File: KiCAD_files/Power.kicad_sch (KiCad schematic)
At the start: 44 parts, among them J101 Wago 6 contacts, P101 Power2, U101 AMC1311, U102 MCP6486UT-E/LT, U103 MCP6486UT-E/LT, U104 ACS723LLCTR-20AB

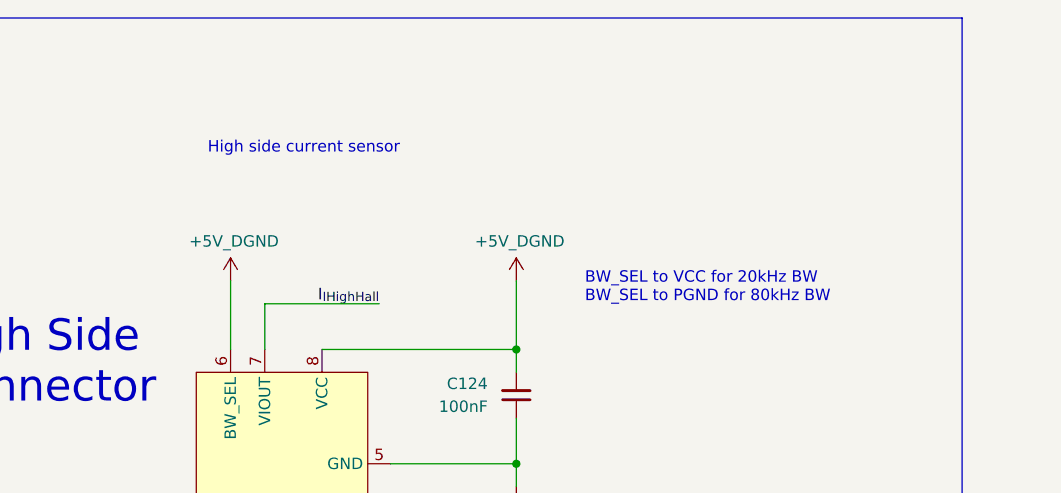
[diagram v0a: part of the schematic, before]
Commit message: better comments for ACS723 high side current sensor
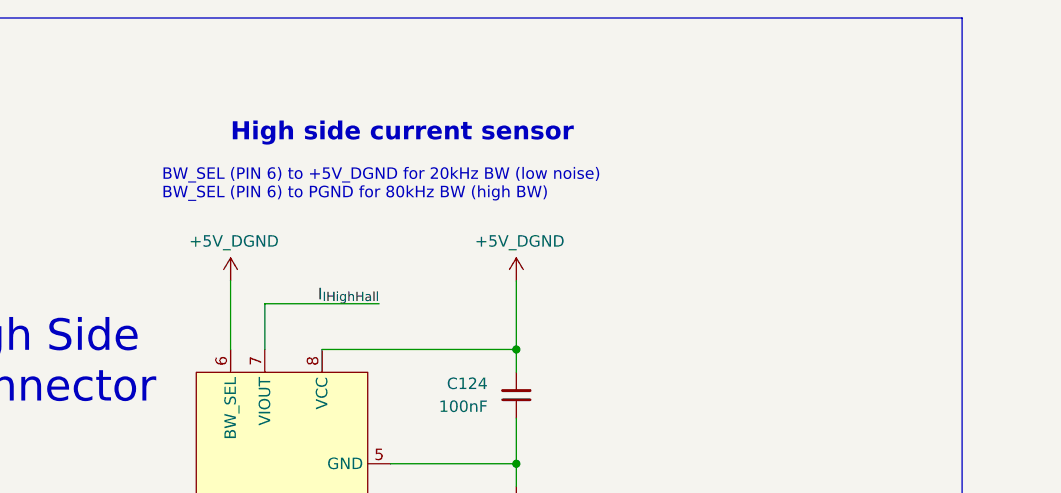
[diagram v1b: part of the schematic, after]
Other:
- note added: "BW_SEL (PIN 6) to +5V_DGND for 20kHz BW (low noise) BW_SEL (PIN 6) to PGND for 80kHz BW (high BW)"
- note removed: "BW_SEL to VCC for 20kHz BW BW_SEL to PGND for 80kHz BW"
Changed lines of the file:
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@@
     (effects (font (size 1.27 1.27)) (justify left bottom))
   )
-  (text "High side current sensor" (at 207.01 29.21 0)
-    (effects (font (size 1.27 1.27)) (justify left bottom))
+  (text "High side current sensor" (at 209.55 27.94 0)
+    (effects (font (size 2 2) (thickness 0.4) bold) (justify left bottom))
   )
   (text "V_High has no offset \nas V_High is solely positive\n"
@@
     (effects (font (size 1.27 1.27)) (justify left bottom))
   )
-  (text "BW_SEL to VCC for 20kHz BW\nBW_SEL to PGND for 80kHz BW"
-    (at 248.92 45.72 0)
+  (text "BW_SEL (PIN 6) to +5V_DGND for 20kHz BW (low noise)\nBW_SEL (PIN 6) to PGND for 80kHz BW (high BW)"
+    (at 201.93 34.29 0)
     (effects (font (size 1.27 1.27)) (justify left bottom))
   )

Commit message: wip SHEMATIC
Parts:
- removed C101, C102, C124: 100nF, Capacitor_SMD:C_1206_3216Metric, symbol Device:C_Small
- removed C103, C117, C123: 100nF, Footprints:C_0805_2012Metric, symbol Device:C_Small
- removed C106, C119: 20pF, Footprints:C_0805_2012Metric, symbol Device:C_Small
- removed R103, R104, R105, R107: 27k, Footprints:R_0805_2012Metric, symbol Device:R_Small
- removed R110, R116: 5.9k, Footprints:R_0805_2012Metric, symbol Device:R_Small
- removed R111, R115: 20k, Footprints:R_0805_2012Metric, symbol Device:R_Small
- removed R117: 330k, Footprints:R_0805_2012Metric, symbol Device:R_Small
- removed R118: 5.6k, Footprints:R_0805_2012Metric, symbol Device:R_Small
- removed TP101, TP102, TP103, TP104, TP105, TP106, TP107: TestPoint, Footprints:TestPoint_THTPad_D1.5mm_Drill0.7mm, symbol Connector:TestPoint
- removed U101: AMC1311, Footprints:SOIC-8_7.5x5.85mm_P1.27mm, symbol Symbols:AMC1311
- removed U102, U103: MCP6486UT-E/LT, Package_TO_SOT_SMD:SOT-353_SC-70-5_Handsoldering, symbol Amplifier_Operational:TLV6001DCK
- removed U104: ACS723LLCTR-20AB, Package_SO:SOIC-8_3.9x4.9mm_P1.27mm, symbol Symbols:ACS723
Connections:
- net NGND is gone; now on net PGND: J101.14 (Pin_4), J101.6 (Pin_1), J101.7 (Pin_2), J101.8 (Pin_3)
- net High_side/V_{IHighOutFused_PGND}: now reaches F103.2, J101.1 (Pin_1)
- net V1_Low renamed V1_Low_PGND
- net V2_Low renamed V2_Low_PGND
- net V_{IHighOut} renamed V_{IHighOut_PGND}
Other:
- sheet Digital renamed MCU
- added sheet High_side (High_side.kicad_sch)
- sheet Feeder ports: added VIN_PGND, Vref_DGND; removed +5V_NEUTRAL, VIN, VRef
- sheet MCU ports: added +3.3V_DGND, HRTIM_CHA1_DGND, HRTIM_CHA2_DGND, HRTIM_CHC1_DGND, HRTIM_CHC2_DGND, I_{I1Low_DGND}, I_{I2Low_DGND}, I_{IHigh_sense_DGND}, V_{I1Low_DGND}, V_{I2Low_DGND}, V_{IHigh_sense_DGND}, ~{STBY1}_DGND, ~{STBY2}_DGND; removed HRTIM_CHA1, HRTIM_CHA2, HRTIM_CHC1, HRTIM_CHC2, I_{I1Low}, I_{I2Low}, I_{IHigh}, N_{PGND}, VREF, V_{I1Low}, V_{I2Low}, V_{IHighfeeder}, V_{IHigh}, ~{STBY1}, ~{STBY2}
- sheet Power Leg 1 ports: added HRTIM_HIGH_DGND, HRTIM_LOW_DGND, I_{ILow_DGND}, V_High_PGND, V_Low_PGND, V_{ILow_DGND}, ~{STBY}_DGND; removed HRTIM1_CH1, HRTIM1_CH2, I_{ILow}, N_{PGND}, VRef, V_High, V_Low, V_{ILow}, ~{STBY}
- sheet Power Leg 2 ports: added HRTIM_HIGH_DGND, HRTIM_LOW_DGND, I_{ILow_DGND}, V_High_PGND, V_Low_PGND, V_{ILow_DGND}, ~{STBY}_DGND; removed HRTIM1_CH1, HRTIM1_CH2, I_{ILow}, N_{PGND}, VRef, V_High, V_Low, V_{ILow}, ~{STBY}
- note added: "All resistor are thick film 1/8Watt unless specified"
- note added: "High Side"
- note added: "designator base 200"
- note added: "designator base 300"
- note added: "designator base 400"
- note added: "designator base 500"
- note added: "designator base 600"
- note removed: "All resistor to are thick film 1/8Watt unless specified"
- note removed: "BW_SEL (PIN 6) to +5V_DGND for 20kHz BW (low noise) BW_SEL (PIN 6) to PGND for 80kHz BW (high BW)"
- note removed: "Circuit can be seen as non inverting opamp with gain : G = 1+(RC/RD) and a potential on non-inverting input equal to V+=(VOUTP-VOUTN) multiplied by the ratio of voltage divider equal to : r = RB/(RA+RB)"
- note removed: "Current measurements 5V to 2.048"
- note removed: "Gain : 1"
- note removed: "High Side Current Measure"
- note removed: "High Side Voltage Measure"
- note removed: "High Side voltage measurement"
- note removed: "High side current sensor"
- note removed: "NEUTRAL AREA"
- note removed: "RA"
- note removed: "RB"
- note removed: "RC"
- note removed: "RD"
- note removed: "RE"
- note removed: "RF"
- note removed: "RG"
- note removed: "RH"
- note removed: "Simulation available https://tinyurl.com/2k73em8x"
- note removed: "VI_High_op has a 2,048V amplitude without offset"
- note removed: "V_High has no offset as V_High is solely positive"
- note removed: "V_{SHIFTED} = ((RE + RF)*RH / (RH + RG)*RF) * I_{IHigh} - (RE/RF)* 5V_{Digital} V_{SHIFTED} = ((5.9k + 20k)*20k / (20k + 5.9k)*20k) * I_{IHigh} - (5.9k/20k)* 5V_{Digital} V_{SHIFTED} = I_{IHigh} - (5.9k/20k)* 5V_{Digital} V_{SHIFTED} = I_{IHigh} - 1.5V ** If RH = RF and RE = RG, gain is unitary"
- note removed: "https://www.allegromicro.com/en/Insights-and-Innovations/ Technical-Documents/Hall-Effect-Sensor-IC-Publications/ Shifting-the-Offset-Voltage-of-Current-Sensors"
- note removed: "https://www.falstad.com/circuit/circuitjs.html"
- company: https://gitlab.laas.fr/owntech/1leg/-/tree/V1.1.1/KiCAD_files -> https://gitlab.laas.fr/owntech/boards/TWIST
- moved on the sheet: F101, F102, F103, H101, H102, H103, H104, H105, H106, H107, H108, H109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

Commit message: WIP
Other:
- note removed: "TWIST V1.4"
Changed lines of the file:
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@@
     (effects (font (size 3.5 3.5)) (justify left bottom))
-  )
-  (text "TWIST V1.4" (at 382.27 167.64 0)
-    (effects (font (size 3 3) (thickness 0.6) bold) (justify left bottom))
   )
   (text "designator base 200" (at 80.01 123.19 0)

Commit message: big clean in libraries (imported components in symbol), PCB WIP
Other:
- sheet MCU ports: added LEG1_CAPA_DRIVE_DGND, LEG2_CAPA_DRIVE_DGND; removed none
- sheet Power Leg 1 ports: added LEG_CAPA_DRIVE_DGND; removed none
- sheet Power Leg 2 ports: added LEG_CAPA_DRIVE_DGND; removed none
- moved on the sheet: F101, F102, J101D, J101E, J101G, J101H

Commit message: Ready for design review
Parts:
- J101: value Wago 6 contacts -> Harting - 15contacts and Wago
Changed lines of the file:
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@@
     )
   )
-  (symbol (lib_id "Symbols:Harting 15 contacts and WAGO") (at 36.83 100.33 0) (mirror y) (unit 8)
+  (symbol (lib_name "Harting 15 contacts and WAGO_1") (lib_id "Symbols:Harting 15 contacts and WAGO") (at 36.83 100.33 0) (mirror y) (unit 8)
     (in_bom yes) (on_board yes) (dnp no)
-    (property "Reference" "J101" (at 30.48 100.33 0)
-      (effects (font (size 1.27 1.27)))
-    )
-    (property "Value" "Wago 6 contacts" (at 38.1 114.3 0)
+    (property "Reference" "J101" (at 34.29 101.6 0)
+      (effects (font (size 1.27 1.27)) (justify left))
+    )
+    (property "Value" "Harting - 15contacts and Wago" (at 38.1 114.3 0)
       (effects (font (size 1.27 1.27)) hide)
     )
@@
     )
   )
-  (symbol (lib_id "Symbols:Harting 15 contacts and WAGO") (at 36.83 144.78 0) (mirror y) (unit 4)
+  (symbol (lib_name "Harting 15 contacts and WAGO_1") (lib_id "Symbols:Harting 15 contacts and WAGO") (at 36.83 144.78 0) (mirror y) (unit 4)
     (in_bom yes) (on_board yes) (dnp no)
-    (property "Reference" "J101" (at 30.48 144.78 0)
-      (effects (font (size 1.27 1.27)))
-    )
-    (property "Value" "Wago 6 contacts" (at 38.1 158.75 0)
+    (property "Reference" "J101" (at 34.29 146.05 0)
+      (effects (font (size 1.27 1.27)) (justify left))
+    )
+    (property "Value" "Harting - 15contacts and Wago" (at 38.1 158.75 0)
       (effects (font (size 1.27 1.27)) hide)
     )
@@
     )
   )
-  (symbol (lib_id "Symbols:Harting 15 contacts and WAGO") (at 276.86 100.33 0) (unit 6)
+  (symbol (lib_name "Harting 15 contacts and WAGO_1") (lib_id "Symbols:Harting 15 contacts and WAGO") (at 276.86 100.33 0) (unit 6)
     (in_bom yes) (on_board yes) (dnp no)
-    (property "Reference" "J101" (at 283.21 100.33 0)
-      (effects (font (size 1.27 1.27)))
-    )
-    (property "Value" "Wago 6 contacts" (at 275.59 114.3 0)
+    (property "Reference" "J101" (at 279.4 101.6 0)
+      (effects (font (size 1.27 1.27)) (justify left))
+    )
+    (property "Value" "Harting - 15contacts and Wago" (at 275.59 114.3 0)
       (effects (font (size 1.27 1.27)) hide)
     )
@@
   (symbol (lib_id "Symbols:Harting 15 contacts and WAGO") (at 276.86 132.08 0) (mirror x) (unit 3)
     (in_bom yes) (on_board yes) (dnp no) (fields_autoplaced)
-    (property "Reference" "J101" (at 279.4 128.27 0)
-      (effects (font (size 1.27 1.27)) (justify left))
-    )
-    (property "Value" "Wago 6 contacts" (at 275.59 118.11 0)
+    (property "Reference" "J101" (at 279.4 130.81 0)
+      (effects (font (size 1.27 1.27)) (justify left))
+    )
+    (property "Value" "Harting - 15contacts and Wago" (at 275.59 118.11 0)
       (effects (font (size 1.27 1.27)) hide)
     )
@@
     )
   )
-  (symbol (lib_id "Symbols:Harting 15 contacts and WAGO") (at 36.83 90.17 0) (mirror y) (unit 5)
+  (symbol (lib_name "Harting 15 contacts and WAGO_1") (lib_id "Symbols:Harting 15 contacts and WAGO") (at 36.83 90.17 0) (mirror y) (unit 5)
     (in_bom yes) (on_board yes) (dnp no)
-    (property "Reference" "J101" (at 30.48 88.9 0)
-      (effects (font (size 1.27 1.27)))
-    )
-    (property "Value" "Wago 6 contacts" (at 38.1 104.14 0)
+    (property "Reference" "J101" (at 34.29 91.44 0)
+      (effects (font (size 1.27 1.27)) (justify left))
+    )
+    (property "Value" "Harting - 15contacts and Wago" (at 38.1 104.14 0)
       (effects (font (size 1.27 1.27)) hide)
     )
@@
       (effects (font (size 1.27 1.27)) (justify left))
     )
-    (property "Value" "Wago 6 contacts" (at 275.59 121.92 0)
+    (property "Value" "Harting - 15contacts and Wago" (at 275.59 121.92 0)
       (effects (font (size 1.27 1.27)) hide)
     )
@@
     )
   )
-  (symbol (lib_id "Symbols:Harting 15 contacts and WAGO") (at 276.86 90.17 0) (unit 1)
+  (symbol (lib_name "Harting 15 contacts and WAGO_1") (lib_id "Symbols:Harting 15 contacts and WAGO") (at 276.86 90.17 0) (unit 1)
     (in_bom yes) (on_board yes) (dnp no)
-    (property "Reference" "J101" (at 280.67 91.44 0)
-      (effects (font (size 1.27 1.27)) (justify left))
-    )
-    (property "Value" "Wago 6 contacts" (at 275.59 104.14 0)
+    (property "Reference" "J101" (at 279.4 91.44 0)
+      (effects (font (size 1.27 1.27)) (justify left))
+    )
+    (property "Value" "Harting - 15contacts and Wago" (at 275.59 104.14 0)
       (effects (font (size 1.27 1.27)) hide)
     )
@@
     )
   )
-  (symbol (lib_id "Symbols:Harting 15 contacts and WAGO") (at 36.83 153.67 0) (mirror y) (unit 7)
+  (symbol (lib_name "Harting 15 contacts and WAGO_1") (lib_id "Symbols:Harting 15 contacts and WAGO") (at 36.83 153.67 0) (mirror y) (unit 7)
     (in_bom yes) (on_board yes) (dnp no)
-    (property "Reference" "J101" (at 30.48 153.67 0)
-      (effects (font (size 1.27 1.27)))
-    )
-    (property "Value" "Wago 6 contacts" (at 38.1 167.64 0)
-      (effects (font (size 1.27 1.27)) hide)
-    )
+    (property "Reference" "J101" (at 34.29 154.94 0)
+      (effects (font (size 1.27 1.27)) (justify left))
+    )
+    (property "Value" "Harting - 15contacts and Wago" (at 38.1 167.64 0)
+      (effects (font (size 1.27 1.27)) hide)
+    )

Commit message: ready for design review
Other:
- moved on the sheet: H101, H102, H103, H104, H105, H106, H107, H108, H109, N101

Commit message: wip
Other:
- note added: "All ceramic capacitor are 0805 X7R 50V unless specified"
- note added: "All resistor are 0805 thick film 1/8Watt unless specified"
- note removed: "All ceramic capacitor are X7R 50V unless specified"
- note removed: "All resistor are thick film 1/8Watt unless specified"
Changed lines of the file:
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@@
     (effects (font (size 1.27 1.27)) (justify left bottom))
   )
-  (text "All resistor are thick film 1/8Watt unless specified"
+  (text "All resistor are 0805 thick film 1/8Watt unless specified"
     (at 302.26 168.91 0)
     (effects (font (size 1.27 1.27)) (justify left bottom))
@@
     (effects (font (size 1.27 1.27)) (justify left bottom))
   )
-  (text "All ceramic capacitor are X7R 50V unless specified"
+  (text "All ceramic capacitor are 0805 X7R 50V unless specified"
     (at 302.26 166.37 0)
     (effects (font (size 1.27 1.27)) (justify left bottom))
@@
     (effects (font (size 1.27 1.27)) (justify right bottom))
   )
-  (global_label "Vref_DGND" (shape input) (at 241.3 163.83 0) (fields_autoplaced)
+  (global_label "Vref_DGND" (shape output) (at 241.3 163.83 0) (fields_autoplaced)
     (effects (font (size 1.27 1.27)) (justify left))
     (property "Intersheetrefs" "${INTERSHEET_REFS}" (at 253.3488 163.83 0)

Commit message: wip
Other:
- note added: "All resistor are 0805 thick film 1/8 Watt unless specified"
- note removed: "All resistor are 0805 thick film 1/8Watt unless specified"
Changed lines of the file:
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@@
     (stroke (width 0) (type default))
   )
-  (rectangle (start 21.59 13.97) (end 290.83 209.55)
+  (rectangle (start 21.59 13.97) (end 289.56 208.28)
     (stroke (width 0) (type default))
     (fill (type none))
@@
     (effects (font (size 1.27 1.27)) (justify left bottom))
   )
-  (text "All resistor are 0805 thick film 1/8Watt unless specified"
+  (text "All resistor are 0805 thick film 1/8 Watt unless specified"
     (at 302.26 168.91 0)
     (effects (font (size 1.27 1.27)) (justify left bottom))
@@
     (effects (font (size 1.27 1.27)) (justify left bottom))
   )
-  (text "Power Leg 1" (at 86.36 80.01 0)
+  (text "Power Leg 1" (at 85.09 78.74 0)
     (effects (font (size 3.5 3.5)) (justify left bottom))
   )
@@
     (effects (font (size 1.27 1.27)) (justify left bottom))
   )
-  (text "Power Leg 2\n" (at 87.63 133.35 0)
+  (text "Power Leg 2\n" (at 83.82 132.08 0)
     (effects (font (size 3.5 3.5)) (justify left bottom))
   )
@@
     (effects (font (size 1.27 1.27)) (justify left bottom))
   )
-  (text "High Side\n" (at 196.85 81.28 0)
+  (text "High Side\n" (at 196.85 80.01 0)
     (effects (font (size 3.5 3.5)) (justify left bottom))
   )
